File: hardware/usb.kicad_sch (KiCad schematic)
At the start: 5 parts, among them J2 USB4155-03-C_REVA

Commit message: docs(sheet): update title of schematic sheets
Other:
- company: (none) -> Chaos
- title: (none) -> LBD (Lott-Bespitting Diode)
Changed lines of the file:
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@@
 	(generator_version "10.0")
 	(paper "A4")
+	(title_block
+		(title "LBD (Lott-Bespitting Diode)")
+		(date "2026-06-27")
+		(rev "v1.0")
+		(company "Chaos")
+	)
 	(junction
 		(at 166.37 104.14)

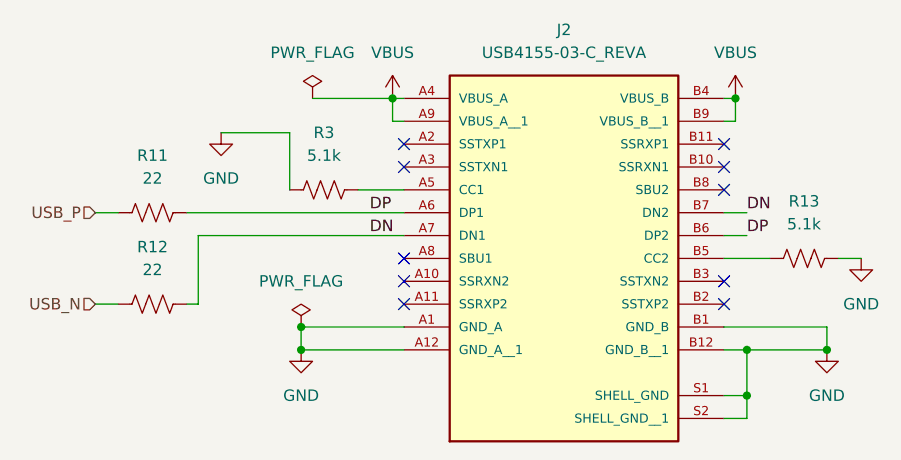
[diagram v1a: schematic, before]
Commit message: fix: remove REV_A suffix from schematic symbol
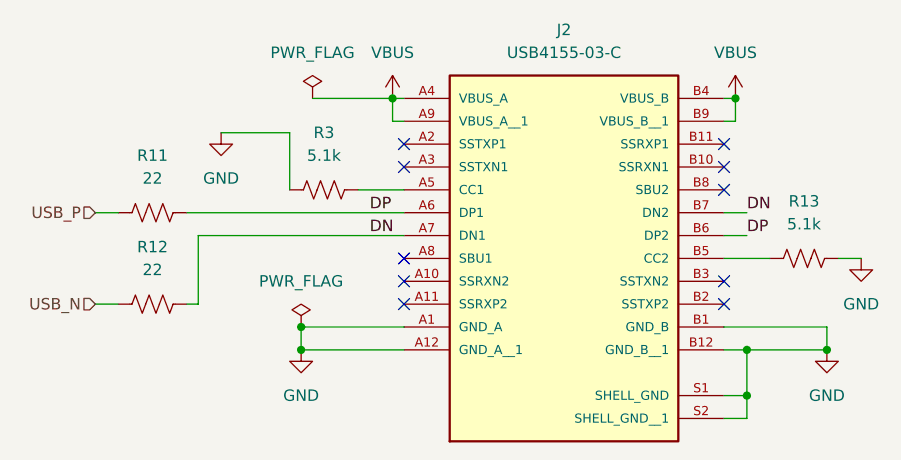
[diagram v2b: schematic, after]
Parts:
- J2: value USB4155-03-C_REVA -> USB4155-03-C
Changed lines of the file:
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@@
 			)
 		)
-		(property "Value" "USB4155-03-C_REVA"
+		(property "Value" "USB4155-03-C"
 			(at 137.16 71.12 0)
 			(show_name no)
